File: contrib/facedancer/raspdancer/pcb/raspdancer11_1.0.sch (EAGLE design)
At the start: 15 parts, among them Q1 12Mhz

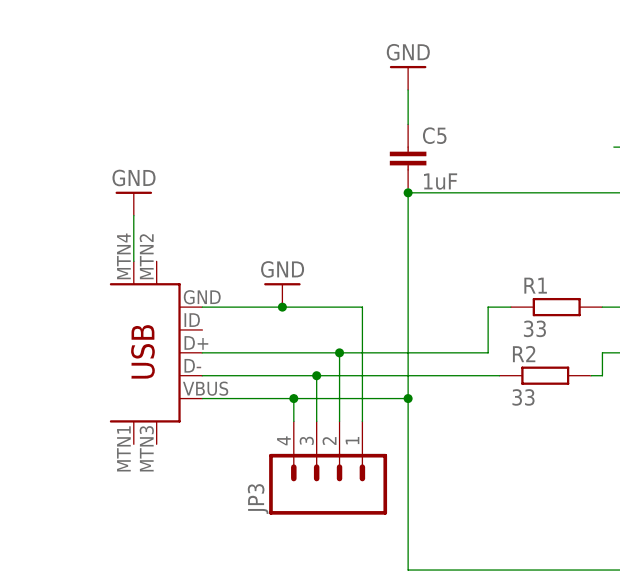
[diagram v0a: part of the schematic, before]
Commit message: raspdancer11 board: more room around IC and other small changes
git-svn-id: https://svn.code.sf.net/p/goodfet/code@1586 12e2690d-a6be-4b82-a7b7-67c4a43b65c8
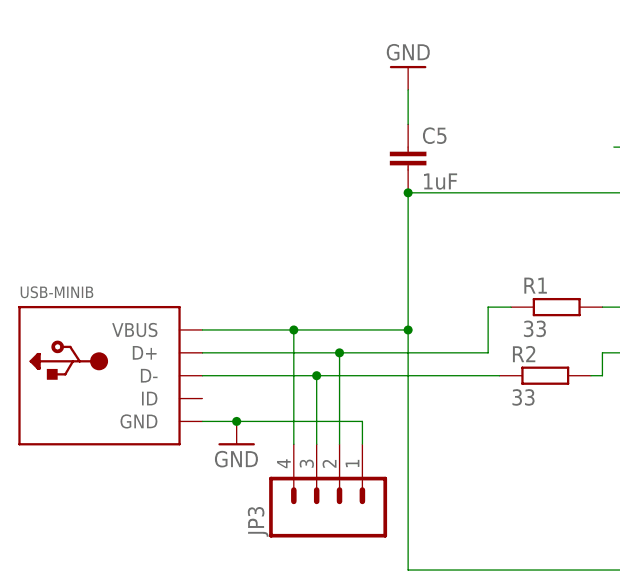
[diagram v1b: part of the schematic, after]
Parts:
- removed USB: USB-MINIB-5PIN, SparkFun:USB-MINIB-5PIN
- added USB-MINIB: (no value), adafruit:USBMINIB
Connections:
- net N$1 renamed D+
- net N$10 renamed GPX2
- net N$11 renamed GPX
- net N$13 renamed VBUS2
- net N$2 renamed IX
- net N$3 renamed XO
- net N$7 renamed D-
- net N$9 renamed INT2
- removed net N$4: C5.2, IC1.VBCOMP, JP1.1, JP3.4, USB.VBUS
- removed net N$5: JP3.2, R1.1, USB.D+
- removed net N$6: JP3.3, R2.1, USB.D-
- new net D+2: JP3.2, R1.1, USB-MINIB.D+
- new net D-2: JP3.3, R2.1, USB-MINIB.D-
- new net VBUS: C5.2, IC1.VBCOMP, JP1.1, JP3.4, USB-MINIB.VBUS
- net GND: no longer USB.GND, USB.MTN4
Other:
- moved on the sheet: JP3
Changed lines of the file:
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@@
 <setting verticaltext="up"/>
 </settings>
-<grid distance="0.05" unitdist="inch" unit="inch" style="lines" multiple="1" display="no" altdistance="0.01" altunitdist="inch" altunit="inch"/>
+<grid distance="0.1" unitdist="inch" unit="inch" style="lines" multiple="1" display="no" altdistance="0.01" altunitdist="inch" altunit="inch"/>
 <layers>
 <layer number="1" name="Top" color="4" fill="1" visible="no" active="no"/>
@@
 <layer number="106" name="bPlate" color="7" fill="1" visible="no" active="yes"/>
 <layer number="107" name="Crop" color="7" fill="1" visible="no" active="yes"/>
+<layer number="108" name="fp8" color="7" fill="1" visible="no" active="yes"/>
+<layer number="109" name="fp9" color="7" fill="1" visible="no" active="yes"/>
+<layer number="110" name="fp0" color="7" fill="1" visible="no" active="yes"/>
+<layer number="111" name="LPC17xx" color="7" fill="1" visible="yes" active="yes"/>
+<layer number="112" name="tSilk" color="7" fill="1" visible="yes" active="yes"/>
 <layer number="116" name="Patch_BOT" color="9" fill="4" visible="no" active="yes"/>
 <layer number="121" name="_tsilk" color="7" fill="1" visible="no" active="yes"/>
 <layer number="122" name="_bsilk" color="7" fill="1" visible="no" active="yes"/>
+<layer number="123" name="tTestmark" color="7" fill="1" visible="no" active="yes"/>
+<layer number="124" name="bTestmark" color="7" fill="1" visible="no" active="yes"/>
 <layer number="125" name="_tNames" color="7" fill="1" visible="no" active="yes"/>
+<layer number="126" name="_bNames" color="7" fill="1" visible="yes" active="yes"/>
+<layer number="127" name="_tValues" color="7" fill="1" visible="yes" active="yes"/>
+<layer number="128" name="_bValues" color="7" fill="1" visible="yes" active="yes"/>
+<layer number="131" name="tAdjust" color="7" fill="1" visible="no" active="yes"/>
+<layer number="132" name="bAdjust" color="7" fill="1" visible="no" active="yes"/>
 <layer number="144" name="Drill_legend" color="7" fill="1" visible="no" active="yes"/>
 <layer number="151" name="HeatSink" color="7" fill="1" visible="no" active="yes"/>
+<layer number="152" name="_bDocu" color="7" fill="1" visible="yes" active="yes"/>
+<layer number="199" name="Contour" color="7" fill="1" visible="yes" active="yes"/>
 <layer number="200" name="200bmp" color="1" fill="10" visible="no" active="yes"/>
 <layer number="201" name="201bmp" color="2" fill="10" visible="no" active="yes"/>
@@
 <layer number="232" name="Eagle3D_PG2" color="7" fill="1" visible="yes" active="yes"/>
 <layer number="233" name="Eagle3D_PG3" color="7" fill="1" visible="yes" active="yes"/>
+<layer number="248" name="Housing" color="7" fill="1" visible="yes" active="yes"/>
+<layer number="249" name="Edge" color="7" fill="1" visible="yes" active="yes"/>
 <layer number="250" name="Descript" color="3" fill="1" visible="no" active="no"/>
 <layer number="251" name="SMDround" color="12" fill="11" visible="no" active="no"/>
@@
 <part name="C3" library="00_mylib" deviceset="C" device="1206" value="18pF"/>
 <part name="C4" library="00_mylib" deviceset="C" device="1206" value="18pF"/>
-<part name="USB" library="SparkFun" deviceset="USB-MINIB" device="-5PIN"/>
 <part name="GND5" library="supply1" deviceset="GND" device=""/>
-<part name="GND6" library="supply1" deviceset="GND" device=""/>
 <part name="GND8" library="supply1" deviceset="GND" device=""/>
 <part name="C5" library="00_mylib" deviceset="C" device="1206" value="1uF"/>
@@
 <part name="GND11" library="supply1" deviceset="GND" device=""/>
 <part name="GND12" library="supply1" deviceset="GND" device=""/>
+<part name="USB-MINIB" library="adafruit" deviceset="USB" device="MINIB"/>
 </parts>
 <sheets>
@@
 <instance part="C3" gate="G$1" x="77.47" y="86.36"/>
 <instance part="C4" gate="G$1" x="90.17" y="86.36"/>
-<instance part="USB" gate="G$1" x="-20.32" y="53.34" rot="R180"/>
-<instance part="GND5" gate="1" x="-8.89" y="55.88" rot="R180"/>
-<instance part="GND6" gate="1" x="-25.4" y="66.04" rot="R180"/>
+<instance part="GND5" gate="1" x="-13.97" y="38.1"/>
 <instance part="GND8" gate="1" x="58.42" y="27.94"/>
 <instance part="C5" gate="G$1" x="5.08" y="68.58"/>
@@
 <instance part="JP1" gate="A" x="132.08" y="50.8"/>
 <instance part="JP2" gate="A" x="104.14" y="81.28" rot="R90"/>
-<instance part="JP3" gate="G$1" x="-2.54" y="35.56" rot="R90"/>
+<instance part="JP3" gate="G$1" x="-2.54" y="33.02" rot="R90"/>
 <instance part="FRAME1" gate="G$1" x="-54.61" y="-36.83"/>
 <instance part="FRAME1" gate="G$2" x="92.71" y="-36.83"/>
@@
 <instance part="GND11" gate="1" x="165.1" y="74.93" rot="R180"/>
 <instance part="GND12" gate="1" x="134.62" y="72.39"/>
+<instance part="USB-MINIB" gate="G$1" x="-27.94" y="45.72"/>
 </instances>
 <busses>
@@
 </segment>
 <segment>
-<wire x1="-8.89" y1="53.34" x2="-17.78" y2="53.34" width="0.1524" layer="91"/>
-<wire x1="0" y1="40.64" x2="0" y2="53.34" width="0.1524" layer="91"/>
-<wire x1="0" y1="53.34" x2="-8.89" y2="53.34" width="0.1524" layer="91"/>
-<junction x="-8.89" y="53.34"/>
-<pinref part="USB" gate="G$1" pin="GND"/>
+<wire x1="-13.97" y1="40.64" x2="-17.78" y2="40.64" width="0.1524" layer="91"/>
+<wire x1="0" y1="38.1" x2="0" y2="40.64" width="0.1524" layer="91"/>
+<wire x1="0" y1="40.64" x2="-13.97" y2="40.64" width="0.1524" layer="91"/>
+<junction x="-13.97" y="40.64"/>
 <pinref part="GND5" gate="1" pin="GND"/>
 <pinref part="JP3" gate="G$1" pin="1"/>
-</segment>
-<segment>
-<wire x1="-25.4" y1="58.42" x2="-25.4" y2="63.5" width="0.1524" layer="91"/>
-<pinref part="USB" gate="G$1" pin="MTN4"/>
-<pinref part="GND6" gate="1" pin="GND"/>
 </segment>
 <segment>
@@
 </segment>
 </net>
-<net name="N$2" class="0">
+<net name="IX" class="0">
 <segment>
 <wire x1="81.28" y1="78.74" x2="81.28" y2="91.44" width="0.1524" layer="91"/>
@@
 </segment>
 </net>
-<net name="N$3" class="0">
+<net name="XO" class="0">
 <segment>
 <wire x1="86.36" y1="91.44" x2="86.36" y2="78.74" width="0.1524" layer="91"/>
@@
 </segment>
 </net>
-<net name="N$4" class="0">
+<net name="VBUS" class="0">
 <segment>
 <wire x1="5.08" y1="66.04" x2="33.02" y2="66.04" width="0.1524" layer="91"/>
-<wire x1="-17.78" y1="43.18" x2="-7.62" y2="43.18" width="0.1524" layer="91"/>
-<wire x1="-7.62" y1="43.18" x2="5.08" y2="43.18" width="0.1524" layer="91"/>
-<wire x1="5.08" y1="43.18" x2="5.08" y2="66.04" width="0.1524" layer="91"/>
-<wire x1="-7.62" y1="40.64" x2="-7.62" y2="43.18" width="0.1524" layer="91"/>
+<wire x1="-7.62" y1="50.8" x2="5.08" y2="50.8" width="0.1524" layer="91"/>
+<wire x1="5.08" y1="50.8" x2="5.08" y2="66.04" width="0.1524" layer="91"/>
+<wire x1="-7.62" y1="38.1" x2="-7.62" y2="50.8" width="0.1524" layer="91"/>
 <wire x1="132.08" y1="43.18" x2="132.08" y2="24.13" width="0.1524" layer="91"/>
 <wire x1="132.08" y1="24.13" x2="5.08" y2="24.13" width="0.1524" layer="91"/>
-<wire x1="5.08" y1="24.13" x2="5.08" y2="43.18" width="0.1524" layer="91"/>
+<wire x1="5.08" y1="24.13" x2="5.08" y2="50.8" width="0.1524" layer="91"/>
 <junction x="5.08" y="66.04"/>
-<junction x="-7.62" y="43.18"/>
-<junction x="5.08" y="43.18"/>
+<junction x="5.08" y="50.8"/>
 <pinref part="IC1" gate="G$1" pin="VBCOMP"/>
-<pinref part="USB" gate="G$1" pin="VBUS"/>
 <pinref part="C5" gate="G$1" pin="2"/>
 <pinref part="JP3" gate="G$1" pin="4"/>
 <pinref part="JP1" gate="A" pin="1"/>
-</segment>
-</net>
-<net name="N$5" class="0">
+<pinref part="USB-MINIB" gate="G$1" pin="VBUS"/>
+<wire x1="-17.78" y1="50.8" x2="-7.62" y2="50.8" width="0.1524" layer="91"/>
+<junction x="-7.62" y="50.8"/>
+</segment>
+</net>
+<net name="D+2" class="0">
 <segment>
 <wire x1="13.97" y1="53.34" x2="16.51" y2="53.34" width="0.1524" layer="91"/>
@@
 <wire x1="-17.78" y1="48.26" x2="-2.54" y2="48.26" width="0.1524" layer="91"/>
 <wire x1="-2.54" y1="48.26" x2="13.97" y2="48.26" width="0.1524" layer="91"/>
-<wire x1="-2.54" y1="40.64" x2="-2.54" y2="48.26" width="0.1524" layer="91"/>
+<wire x1="-2.54" y1="38.1" x2="-2.54" y2="48.26" width="0.1524" layer="91"/>
 <junction x="-2.54" y="48.26"/>
 <pinref part="R1" gate="G$1" pin="1"/>
-<pinref part="USB" gate="G$1" pin="D+"/>
 <pinref part="JP3" gate="G$1" pin="2"/>
-</segment>
-</net>
-<net name="N$6" class="0">
+<pinref part="USB-MINIB" gate="G$1" pin="D+"/>
+</segment>
+</net>
+<net name="D-2" class="0">
 <segment>
 <wire x1="-17.78" y1="45.72" x2="-5.08" y2="45.72" width="0.1524" layer="91"/>
 <wire x1="-5.08" y1="45.72" x2="15.24" y2="45.72" width="0.1524" layer="91"/>
-<wire x1="-5.08" y1="40.64" x2="-5.08" y2="45.72" width="0.1524" layer="91"/>
+<wire x1="-5.08" y1="38.1" x2="-5.08" y2="45.72" width="0.1524" layer="91"/>
 <junction x="-5.08" y="45.72"/>
 <pinref part="R2" gate="G$1" pin="1"/>
-<pinref part="USB" gate="G$1" pin="D-"/>
 <pinref part="JP3" gate="G$1" pin="3"/>
-</segment>
-</net>
-<net name="N$1" class="0">
+<pinref part="USB-MINIB" gate="G$1" pin="D-"/>
+</segment>
+</net>
+<net name="D+" class="0">
 <segment>
 <wire x1="26.67" y1="53.34" x2="33.02" y2="53.34" width="0.1524" layer="91"/>
@@
 </segment>
 </net>
-<net name="N$7" class="0">
+<net name="D-" class="0">
 <segment>
 <wire x1="26.67" y1="48.26" x2="33.02" y2="48.26" width="0.1524" layer="91"/>
@@
 </segment>
 </net>
-<net name="N$13" class="0">
+<net name="VBUS2" class="0">
 <segment>
 <wire x1="157.48" y1="69.85" x2="161.29" y2="69.85" width="0.1524" layer="91"/>
@@
 </segment>
 </net>
-<net name="N$9" class="0">
+<net name="INT2" class="0">
 <segment>
 <pinref part="JP2" gate="A" pin="2"/>
@@
 </segment>
 </net>
-<net name="N$10" class="0">
+<net name="GPX2" class="0">
 <segment>
 <pinref part="JP4" gate="A" pin="2"/>
@@
 </segment>
 </net>
-<net name="N$11" class="0">
+<net name="GPX" class="0">
 <segment>
 <wire x1="118.11" y1="48.26" x2="118.11" y2="62.23" width="0.1524" layer="91"/>
